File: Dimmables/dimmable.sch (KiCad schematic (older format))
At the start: 8 parts, among them CON1 12v, P1 LED, P2 MISC, Q1 IRF540N, U1 LM7805CT, U2 PHOTON

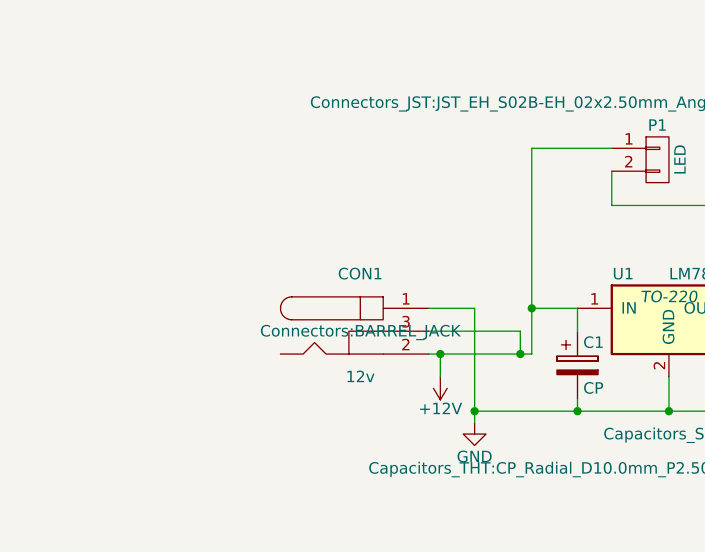
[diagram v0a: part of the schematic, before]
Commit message: production files for wifi dimmer, visual changes
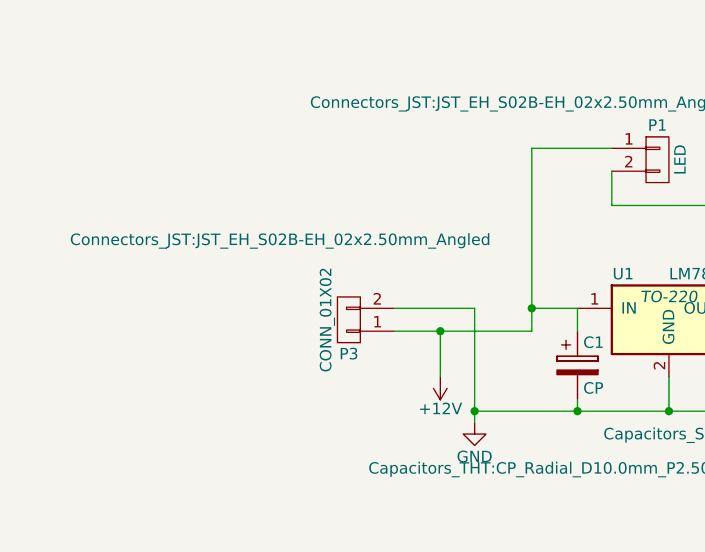
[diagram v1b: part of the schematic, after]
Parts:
- removed CON1: 12v, Connectors:BARREL_JACK, symbol BARREL_JACK
- added P3: CONN_01X02, Connectors_JST:JST_EH_S02B-EH_02x2.50mm_Angled, symbol CONN_01X02
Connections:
- net +12V: now also P3.1 (P1)
- net GND: now also P3.2 (P2)
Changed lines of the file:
@@
-$EndComp
-$Comp
-L BARREL_JACK CON1
-U 1 1 5B47DEAF
-P 3200 2300
-F 0 "CON1" H 3200 2550 50  0000 C CNN
-F 1 "12v" H 3200 2100 50  0000 C CNN
-F 2 "Connectors:BARREL_JACK" H 3200 2300 50  0000 C CNN
-F 3 "" H 3200 2300 50  0000 C CNN
-	1    3200 2300
-	1    0    0    -1
 $EndComp
 $Comp
@@
 	3950 2200 4150 2200
 Wire Wire Line
-	3950 2400 3950 1500
-Wire Wire Line
-	3900 2300 3900 2400
+	3950 2300 3950 1500
 Wire Wire Line
 	3700 2650 5800 2650
@@
 	4950 2650 4950 2600
 Connection ~ 4550 2650
-Wire Wire Line
-	3500 2400 3950 2400
-Connection ~ 3900 2400
 Wire Wire Line
 	3950 1500 4300 1500
@@
 Connection ~ 4150 2650
 Wire Wire Line
-	3900 2300 3500 2300
-Wire Wire Line
-	3500 2200 3700 2200
-Wire Wire Line
 	3700 2200 3700 2700
 $Comp
-L GND #PWR?
+L GND #PWR2
 U 1 1 5B480248
 P 3700 2700
-F 0 "#PWR?" H 3700 2450 50  0001 C CNN
+F 0 "#PWR2" H 3700 2450 50  0001 C CNN
 F 1 "GND" H 3700 2550 50  0000 C CNN
 F 2 "" H 3700 2700 50  0000 C CNN
@@
 Connection ~ 3700 2650
 $Comp
-L +12V #PWR?
+L +12V #PWR1
 U 1 1 5B48051C
 P 3550 2500
-F 0 "#PWR?" H 3550 2350 50  0001 C CNN
+F 0 "#PWR1" H 3550 2350 50  0001 C CNN
 F 1 "+12V" H 3550 2640 50  0000 C CNN
 F 2 "" H 3550 2500 50  0000 C CNN
@@
 $EndComp
 Wire Wire Line
-	3550 2500 3550 2400
-Connection ~ 3550 2400
+	3550 2300 3550 2500
+$Comp
+L CONN_01X02 P3
+U 1 1 5B491D0B
+P 3150 2250
+F 0 "P3" H 3150 2400 50  0000 C CNN
+F 1 "CONN_01X02" V 3250 2250 50  0000 C CNN
+F 2 "Connectors_JST:JST_EH_S02B-EH_02x2.50mm_Angled" H 3450 1900 50  0000 C CNN
+F 3 "" H 3150 2250 50  0000 C CNN
+	1    3150 2250
+	-1   0    0    1
+$EndComp
+Wire Wire Line
+	3350 2300 3950 2300
+Connection ~ 3550 2300
+Wire Wire Line
+	3350 2200 3700 2200
 $EndSCHEMATC
